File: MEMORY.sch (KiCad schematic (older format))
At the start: 2 parts

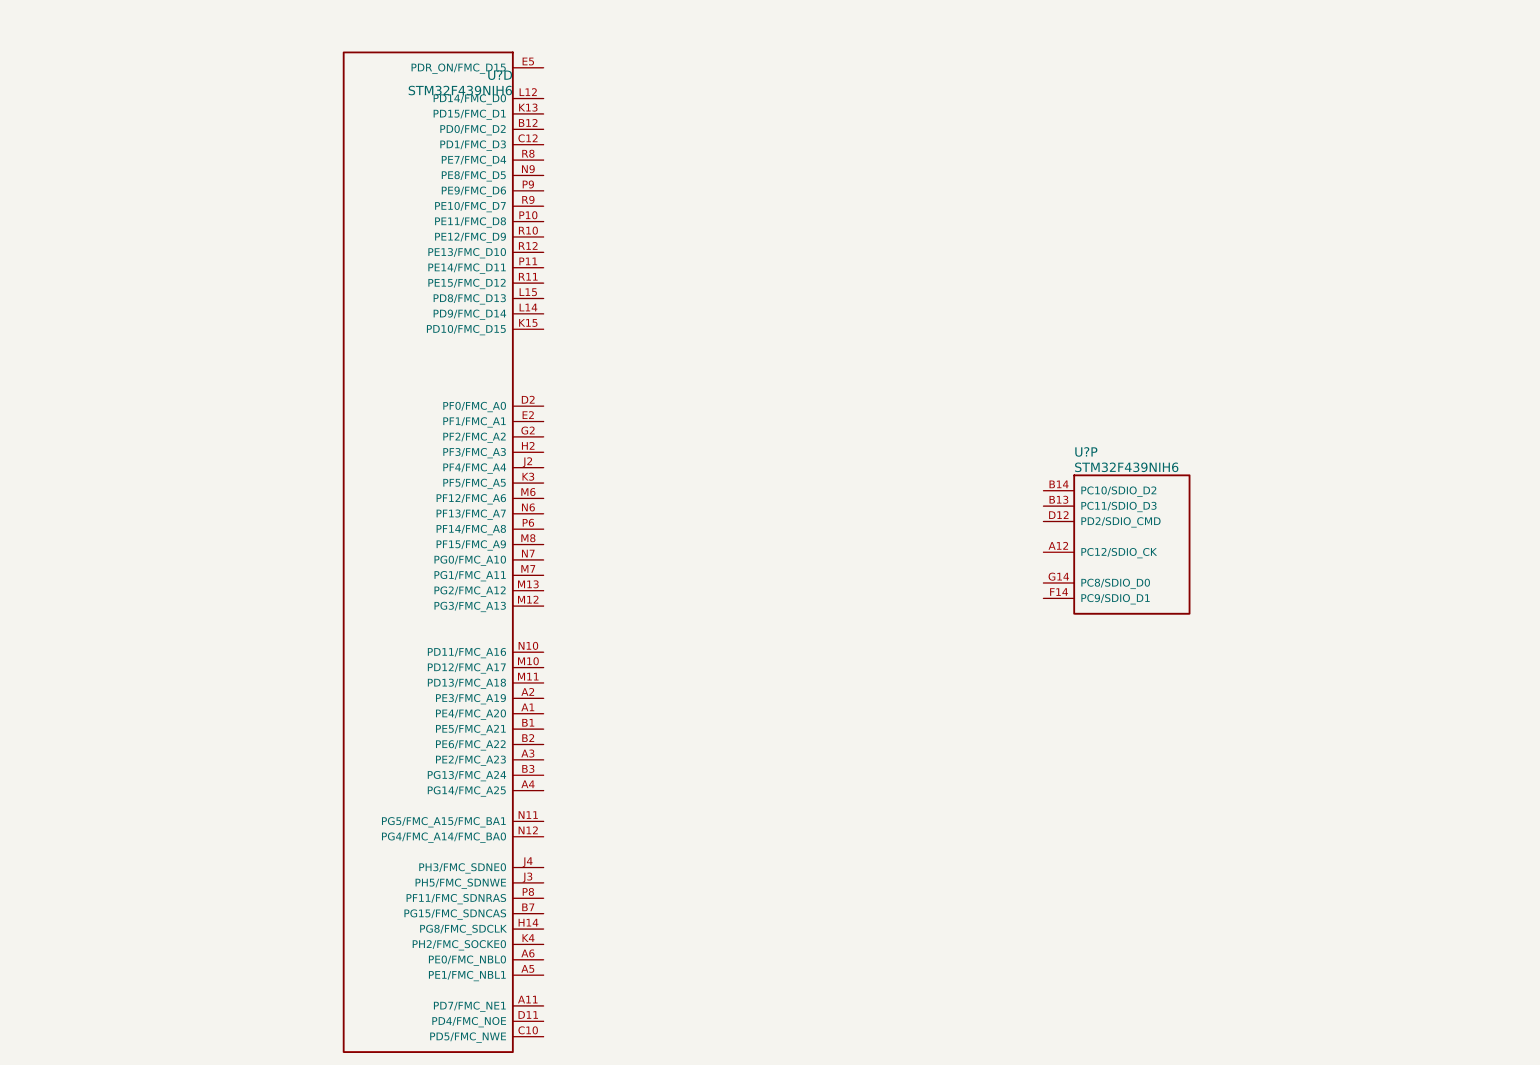
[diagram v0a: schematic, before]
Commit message: current version of the schematics. Audio circuits are still missing.
Audio curcuit topology
Audio from cellphone module is routed to STM
Audio from microphone is routed to STM
STM processes audio and routes microphone data to cellphone module
STM processes audio and routes cellphone audio to amplifier
analog multiplexer can switch route from mic directly to cellphone module and module to speaker
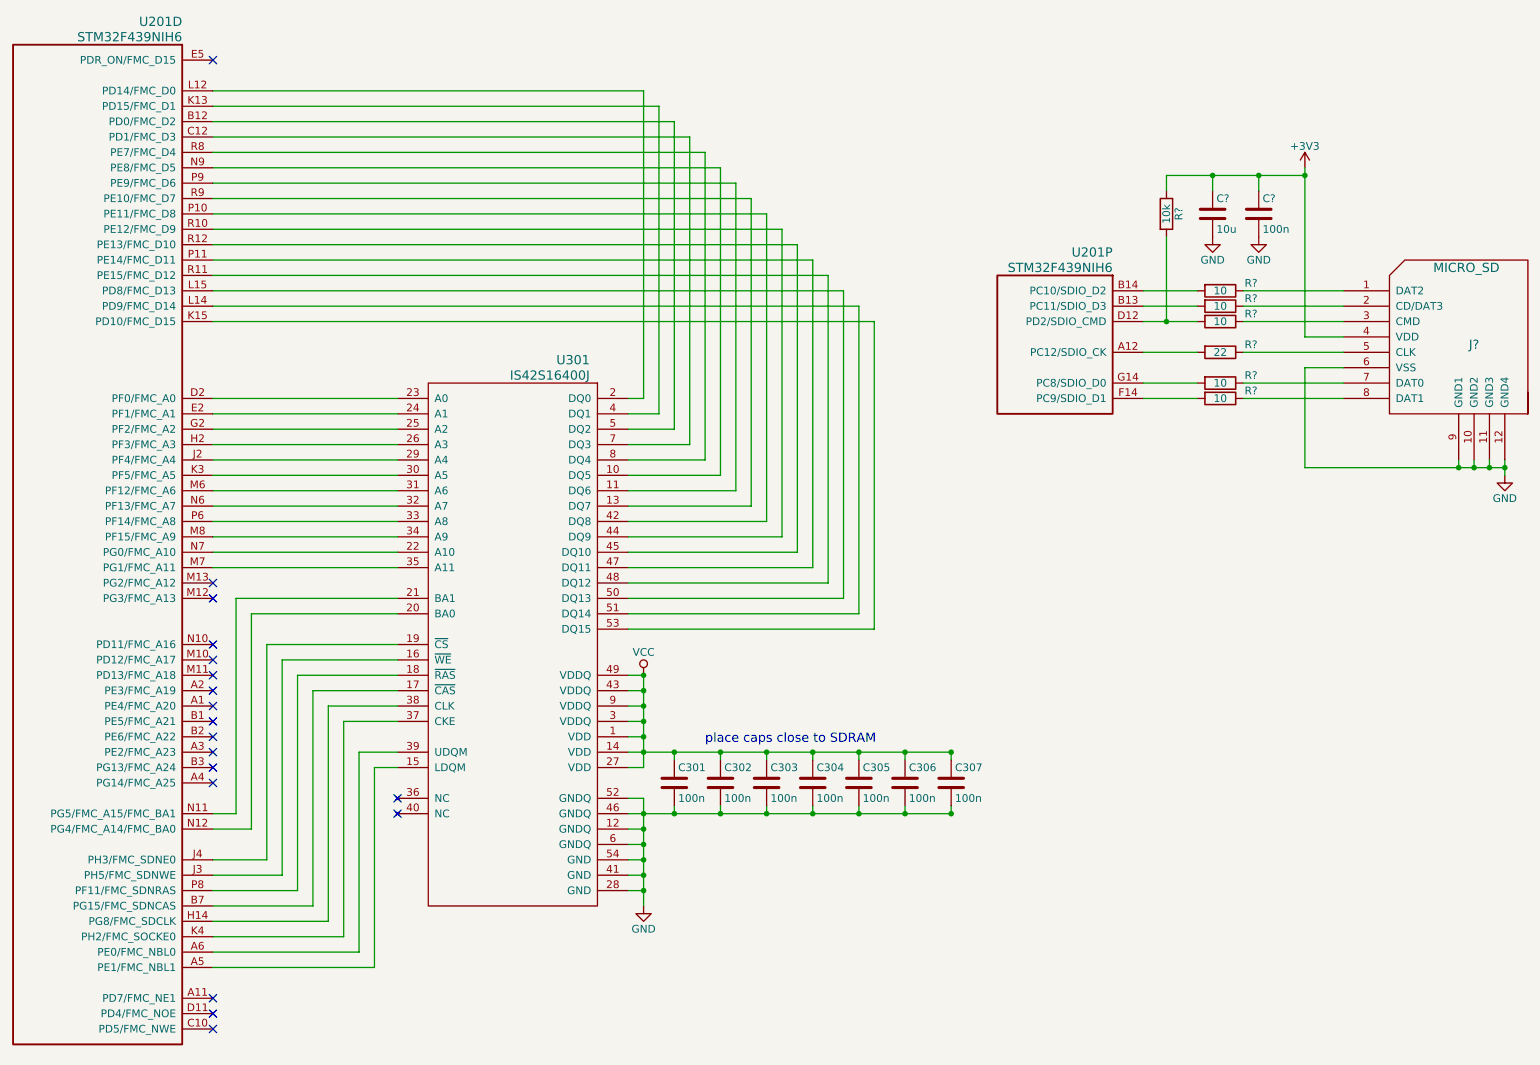
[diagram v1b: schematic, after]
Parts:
- added C301, C302, C303, C304, C305, C306, C307, C?: 100n, symbol C
- added C?: 10u, symbol C
- added J?: MICRO_SD, symbol MICRO_SD
- added R? (x5): 10, symbol R
- added R?: 22, symbol R
- added R?: 10k, symbol R
- added U301: IS42S16400J, symbol IS42S16400J
- gave numbers to parts that had none: 1
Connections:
- net at U201.A12 (PC12/SDIO_CK): now also R?.2
- net at U201.B13 (PC11/SDIO_D3): now also R?.2
- net at U201.B14 (PC10/SDIO_D2): now also R?.2
- net at U201.D12 (PD2/SDIO_CMD): now also R?.2, R?.2
- net at U201.F14 (PC9/SDIO_D1): now also R?.2
- net at U201.G14 (PC8/SDIO_D0): now also R?.2
- net at U201.A5 (PE1/FMC_NBL1): now also U301.15 (LDQM)
- net at U201.A6 (PE0/FMC_NBL0): now also U301.39 (UDQM)
- net at U201.B12 (PD0/FMC_D2): now also U301.5 (DQ2)
- net at U201.B7 (PG15/FMC_SDNCAS): now also U301.17 (~CAS)
- net at U201.C12 (PD1/FMC_D3): now also U301.7 (DQ3)
- net at U201.D2 (PF0/FMC_A0): now also U301.23 (A0)
- net at U201.E2 (PF1/FMC_A1): now also U301.24 (A1)
- net at U201.G2 (PF2/FMC_A2): now also U301.25 (A2)
- net at U201.H14 (PG8/FMC_SDCLK): now also U301.38 (CLK)
- net at U201.H2 (PF3/FMC_A3): now also U301.26 (A3)
- net at U201.J2 (PF4/FMC_A4): now also U301.29 (A4)
- net at U201.J3 (PH5/FMC_SDNWE): now also U301.16 (~WE)
- net at U201.J4 (PH3/FMC_SDNE0): now also U301.19 (~CS)
- net at U201.K13 (PD15/FMC_D1): now also U301.4 (DQ1)
- net at U201.K15 (PD10/FMC_D15): now also U301.53 (DQ15)
- net at U201.K3 (PF5/FMC_A5): now also U301.30 (A5)
- net at U201.K4 (PH2/FMC_SOCKE0): now also U301.37 (CKE)
- net at U201.L12 (PD14/FMC_D0): now also U301.2 (DQ0)
- net at U201.L14 (PD9/FMC_D14): now also U301.51 (DQ14)
- net at U201.L15 (PD8/FMC_D13): now also U301.50 (DQ13)
- net at U201.M6 (PF12/FMC_A6): now also U301.31 (A6)
- net at U201.M7 (PG1/FMC_A11): now also U301.35 (A11)
- net at U201.M8 (PF15/FMC_A9): now also U301.34 (A9)
- net at U201.N11 (PG5/FMC_A15/FMC_BA1): now also U301.21 (BA1)
- net at U201.N12 (PG4/FMC_A14/FMC_BA0): now also U301.20 (BA0)
- net at U201.N6 (PF13/FMC_A7): now also U301.32 (A7)
- net at U201.N7 (PG0/FMC_A10): now also U301.22 (A10)
- net at U201.N9 (PE8/FMC_D5): now also U301.10 (DQ5)
- net at U201.P10 (PE11/FMC_D8): now also U301.42 (DQ8)
- net at U201.P11 (PE14/FMC_D11): now also U301.47 (DQ11)
- net at U201.P6 (PF14/FMC_A8): now also U301.33 (A8)
- net at U201.P8 (PF11/FMC_SDNRAS): now also U301.18 (~RAS)
- net at U201.P9 (PE9/FMC_D6): now also U301.11 (DQ6)
- net at U201.R10 (PE12/FMC_D9): now also U301.44 (DQ9)
- net at U201.R11 (PE15/FMC_D12): now also U301.48 (DQ12)
- net at U201.R12 (PE13/FMC_D10): now also U301.45 (DQ10)
- net at U201.R8 (PE7/FMC_D4): now also U301.8 (DQ4)
- net at U201.R9 (PE10/FMC_D7): now also U301.13 (DQ7)
- new net: J?.1 (DAT2), R?.1
- new net: J?.2 (CD/DAT3), R?.1
- new net: J?.3 (CMD), R?.1
- new net: J?.5 (CLK), R?.1
- new net: J?.7 (DAT0), R?.1
- new net: J?.8 (DAT1), R?.1
- new net +3V3: C?.1, C?.1, J?.4 (VDD), R?.1
- new net GND: C301.2, C302.2, C303.2, C304.2, C305.2, C306.2, C307.2, C?.2, C?.2, J?.10 (GND2), J?.11 (GND3), J?.12 (GND4), J?.6 (VSS), J?.9 (GND1), U301.12 (GNDQ), U301.28 (GND), U301.41 (GND), U301.46 (GNDQ), U301.52 (GNDQ), U301.54 (GND), U301.6 (GNDQ)
- new net VCC: C301.1, C302.1, C303.1, C304.1, C305.1, C306.1, C307.1, U301.1 (VDD), U301.14 (VDD), U301.27 (VDD), U301.3 (VDDQ), U301.43 (VDDQ), U301.49 (VDDQ), U301.9 (VDDQ)
- no-connect marks 0 -> 18
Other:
- note added: "place caps close to SDRAM"
- moved on the sheet: U201D, U201P

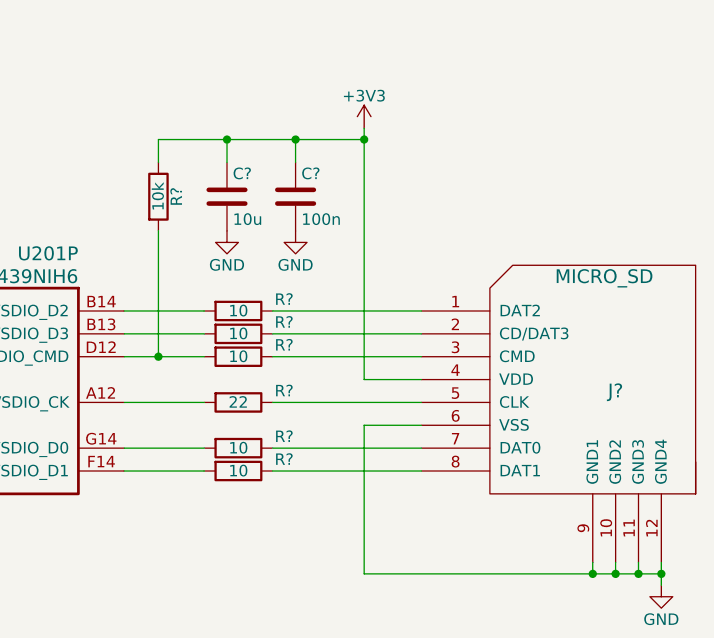
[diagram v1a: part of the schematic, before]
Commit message: added Ti WL1807/1837 Module for WLAN and Bluetooth. added Test Points
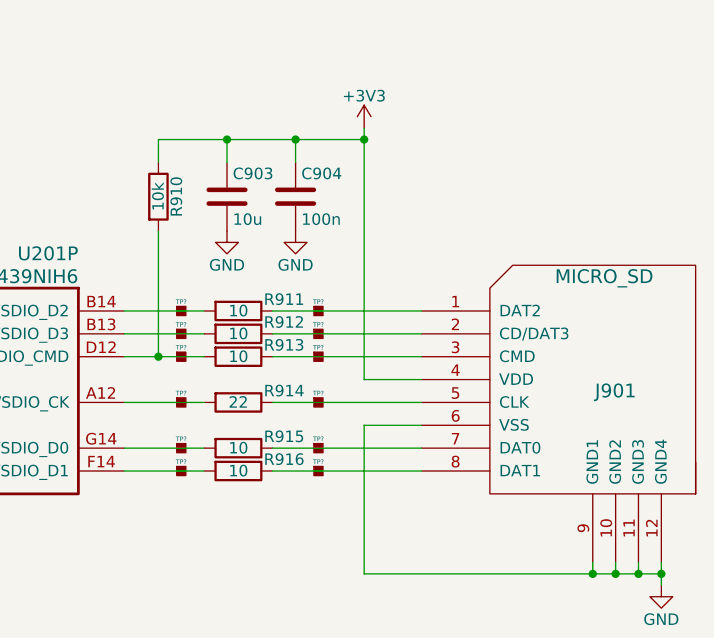
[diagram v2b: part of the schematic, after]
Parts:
- added TP? (x12): TP, symbol TP
- gave numbers to parts that had none: 10
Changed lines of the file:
@@
 LIBS:micro_sd
 LIBS:h144tc215a
-LIBS:3310retro-cache
+LIBS:WL1807MODGIMOCT
+LIBS:tp
+LIBS:w3006
+LIBS:3210retro-cache
 EELAYER 25 0
 EELAYER END
@@
 encoding utf-8
 Sheet 9 9
-Title "Nokia 3310 Retrofit"
-Date "2016-12-08"
+Title "Nokia 3210 Retrofit"
+Date "2016-12-20"
 Rev "1"
 Comp "www.kurzschluss-blog.de"
@@
 Connection ~ 4950 6000
 $Comp
-L GND #PWR302
+L GND #PWR902
 U 1 1 584DBACB
 P 4950 6600
-F 0 "#PWR302" H 4950 6350 50  0001 C CNN
+F 0 "#PWR902" H 4950 6350 50  0001 C CNN
 F 1 "GND" H 4950 6450 50  0000 C CNN
 F 2 "" H 4950 6600 50  0000 C CNN
@@
 Connection ~ 4950 6500
 $Comp
-L VCC #PWR301
+L VCC #PWR901
 U 1 1 584DBB5F
 P 4950 5100
-F 0 "#PWR301" H 4950 4950 50  0001 C CNN
+F 0 "#PWR901" H 4950 4950 50  0001 C CNN
 F 1 "VCC" H 4950 5250 50  0000 C CNN
 F 2 "" H 4950 5100 50  0000 C CNN
@@
 NoConn ~ 2150 7400
 $Comp
-L MICRO_SD J?
+L MICRO_SD J901
 U 1 1 584DD7A8
 P 10300 3000
-F 0 "J?" H 10350 3050 60  0000 C CNN
+F 0 "J901" H 10350 3050 60  0000 C CNN
 F 1 "MICRO_SD" H 10300 3550 60  0000 C CNN
 F 2 "" V 10410 2500 60  0000 C CNN
@@
 $EndComp
 $Comp
-L GND #PWR?
+L GND #PWR906
 U 1 1 584DD873
 P 10550 3800
-F 0 "#PWR?" H 10550 3550 50  0001 C CNN
+F 0 "#PWR906" H 10550 3550 50  0001 C CNN
 F 1 "GND" H 10550 3650 50  0000 C CNN
 F 2 "" H 10550 3800 50  0000 C CNN
@@
 	9500 2600 8850 2600
 $Comp
-L R R?
+L R R911
 U 1 1 584DE0FD
 P 8700 2600
-F 0 "R?" V 8650 2800 50  0000 C CNN
+F 0 "R911" V 8650 2800 50  0000 C CNN
 F 1 "10" V 8700 2600 50  0000 C CNN
 F 2 "" V 8630 2600 50  0000 C CNN
@@
 $EndComp
 $Comp
-L R R?
+L R R912
 U 1 1 584DE1D3
 P 8700 2700
-F 0 "R?" V 8650 2900 50  0000 C CNN
+F 0 "R912" V 8650 2900 50  0000 C CNN
 F 1 "10" V 8700 2700 50  0000 C CNN
 F 2 "" V 8630 2700 50  0000 C CNN
@@
 $EndComp
 $Comp
-L R R?
+L R R913
 U 1 1 584DE20A
 P 8700 2800
-F 0 "R?" V 8650 3000 50  0000 C CNN
+F 0 "R913" V 8650 3000 50  0000 C CNN
 F 1 "10" V 8700 2800 50  0000 C CNN
 F 2 "" V 8630 2800 50  0000 C CNN
@@
 $EndComp
 $Comp
-L R R?
+L R R914
 U 1 1 584DE252
 P 8700 3000
-F 0 "R?" V 8650 3200 50  0000 C CNN
+F 0 "R914" V 8650 3200 50  0000 C CNN
 F 1 "22" V 8700 3000 50  0000 C CNN
 F 2 "" V 8630 3000 50  0000 C CNN
@@
 $EndComp
 $Comp
-L R R?
+L R R915
 U 1 1 584DE2C4
 P 8700 3200
-F 0 "R?" V 8650 3400 50  0000 C CNN
+F 0 "R915" V 8650 3400 50  0000 C CNN
 F 1 "10" V 8700 3200 50  0000 C CNN
 F 2 "" V 8630 3200 50  0000 C CNN
@@
 $EndComp
 $Comp
-L R R?
+L R R916
 U 1 1 584DE318
 P 8700 3300
-F 0 "R?" V 8650 3500 50  0000 C CNN
+F 0 "R916" V 8650 3500 50  0000 C CNN
 F 1 "10" V 8700 3300 50  0000 C CNN
 F 2 "" V 8630 3300 50  0000 C CNN
@@
 	8550 2600 8200 2600
 $Comp
-L +3V3 #PWR?
+L +3V3 #PWR905
 U 1 1 584E0DE7
 P 9250 1800
-F 0 "#PWR?" H 9250 1650 50  0001 C CNN
+F 0 "#PWR905" H 9250 1650 50  0001 C CNN
 F 1 "+3V3" H 9250 1940 50  0000 C CNN
 F 2 "" H 9250 1800 50  0000 C CNN
@@
 $EndComp
 $Comp
-L C C?
+L C C904
 U 1 1 584E0F4B
 P 8950 2100
-F 0 "C?" H 8975 2200 50  0000 L CNN
+F 0 "C904" H 8975 2200 50  0000 L CNN
 F 1 "100n" H 8975 2000 50  0000 L CNN
 F 2 "" H 8988 1950 50  0000 C CNN
@@
 $EndComp
 $Comp
-L C C?
+L C C903
 U 1 1 584E0FEB
 P 8650 2100
-F 0 "C?" H 8675 2200 50  0000 L CNN
+F 0 "C903" H 8675 2200 50  0000 L CNN
 F 1 "10u" H 8675 2000 50  0000 L CNN
 F 2 "" H 8688 1950 50  0000 C CNN
@@
 Connection ~ 8650 1850
 $Comp
-L R R?
+L R R910
 U 1 1 584E1303
 P 8350 2100
-F 0 "R?" V 8430 2100 50  0000 C CNN
+F 0 "R910" V 8430 2100 50  0000 C CNN
 F 1 "10k" V 8350 2100 50  0000 C CNN
 F 2 "" V 8280 2100 50  0000 C CNN
@@
 Connection ~ 8350 2800
 $Comp
-L GND #PWR?
+L GND #PWR904
 U 1 1 584E1578
 P 8950 2250
-F 0 "#PWR?" H 8950 2000 50  0001 C CNN
+F 0 "#PWR904" H 8950 2000 50  0001 C CNN
 F 1 "GND" H 8950 2100 50  0000 C CNN
 F 2 "" H 8950 2250 50  0000 C CNN
@@
 $EndComp
 $Comp
-L GND #PWR?
+L GND #PWR903
 U 1 1 584E15BF
 P 8650 2250
-F 0 "#PWR?" H 8650 2000 50  0001 C CNN
+F 0 "#PWR903" H 8650 2000 50  0001 C CNN
 F 1 "GND" H 8650 2100 50  0000 C CNN
 F 2 "" H 8650 2250 50  0000 C CNN
@@
 NoConn ~ 2150 5800
 NoConn ~ 2150 1100
+$Comp
+L TP TP?
+U 1 1 585C79CD
+P 8450 2600
+F 0 "TP?" H 8450 2640 20  0000 C CNN
+F 1 "TP" H 8450 2550 60  0001 C CNN
+F 2 "" H 8450 2600 60  0000 C CNN
+F 3 "" H 8450 2600 60  0000 C CNN
+	1    8450 2600
+	1    0    0    -1
+$EndComp
+$Comp
+L TP TP?
+U 1 1 585C7A1F
+P 8450 2700
+F 0 "TP?" H 8450 2740 20  0000 C CNN
+F 1 "TP" H 8450 2650 60  0001 C CNN
+F 2 "" H 8450 2700 60  0000 C CNN
+F 3 "" H 8450 2700 60  0000 C CNN
+	1    8450 2700
+	1    0    0    -1
+$EndComp
+$Comp
+L TP TP?
+U 1 1 585C7A75
+P 8450 2800
+F 0 "TP?" H 8450 2840 20  0000 C CNN
+F 1 "TP" H 8450 2750 60  0001 C CNN
+F 2 "" H 8450 2800 60  0000 C CNN
+F 3 "" H 8450 2800 60  0000 C CNN
+	1    8450 2800
+	1    0    0    -1
+$EndComp
+$Comp
+L TP TP?
+U 1 1 585C7ACE
+P 8450 3000
+F 0 "TP?" H 8450 3040 20  0000 C CNN
+F 1 "TP" H 8450 2950 60  0001 C CNN
+F 2 "" H 8450 3000 60  0000 C CNN
+F 3 "" H 8450 3000 60  0000 C CNN
+	1    8450 3000
+	1    0    0    -1
+$EndComp
+$Comp
+L TP TP?
+U 1 1 585C7B32
+P 8450 3200
+F 0 "TP?" H 8450 3240 20  0000 C CNN
+F 1 "TP" H 8450 3150 60  0001 C CNN
+F 2 "" H 8450 3200 60  0000 C CNN
+F 3 "" H 8450 3200 60  0000 C CNN
+	1    8450 3200
+	1    0    0    -1
+$EndComp
+$Comp
+L TP TP?
+U 1 1 585C7B9D
+P 8450 3300
+F 0 "TP?" H 8450 3340 20  0000 C CNN
+F 1 "TP" H 8450 3250 60  0001 C CNN
+F 2 "" H 8450 3300 60  0000 C CNN
+F 3 "" H 8450 3300 60  0000 C CNN
+	1    8450 3300
+	1    0    0    -1
+$EndComp
+$Comp
+L TP TP?
+U 1 1 585C7BFF
+P 9050 3300
+F 0 "TP?" H 9050 3340 20  0000 C CNN
+F 1 "TP" H 9050 3250 60  0001 C CNN
+F 2 "" H 9050 3300 60  0000 C CNN
+F 3 "" H 9050 3300 60  0000 C CNN
+	1    9050 3300
+	1    0    0    -1
+$EndComp
+$Comp
+L TP TP?
+U 1 1 585C7C8C
+P 9050 3200
+F 0 "TP?" H 9050 3240 20  0000 C CNN
+F 1 "TP" H 9050 3150 60  0001 C CNN
+F 2 "" H 9050 3200 60  0000 C CNN
+F 3 "" H 9050 3200 60  0000 C CNN
+	1    9050 3200
+	1    0    0    -1
+$EndComp
+$Comp
+L TP TP?
+U 1 1 585C7D52
+P 9050 3000
+F 0 "TP?" H 9050 3040 20  0000 C CNN
+F 1 "TP" H 9050 2950 60  0001 C CNN
+F 2 "" H 9050 3000 60  0000 C CNN
+F 3 "" H 9050 3000 60  0000 C CNN
+	1    9050 3000
+	1    0    0    -1
+$EndComp
+$Comp
+L TP TP?
+U 1 1 585C7DC5
+P 9050 2800
+F 0 "TP?" H 9050 2840 20  0000 C CNN
+F 1 "TP" H 9050 2750 60  0001 C CNN
+F 2 "" H 9050 2800 60  0000 C CNN
+F 3 "" H 9050 2800 60  0000 C CNN
+	1    9050 2800
+	1    0    0    -1
+$EndComp
+$Comp
+L TP TP?
+U 1 1 585C7EC1
+P 9050 2700
+F 0 "TP?" H 9050 2740 20  0000 C CNN
+F 1 "TP" H 9050 2650 60  0001 C CNN
+F 2 "" H 9050 2700 60  0000 C CNN
+F 3 "" H 9050 2700 60  0000 C CNN
+	1    9050 2700
+	1    0    0    -1
+$EndComp
+$Comp
+L TP TP?
+U 1 1 585C7F32
+P 9050 2600
+F 0 "TP?" H 9050 2640 20  0000 C CNN
+F 1 "TP" H 9050 2550 60  0001 C CNN
+F 2 "" H 9050 2600 60  0000 C CNN
+F 3 "" H 9050 2600 60  0000 C CNN
+	1    9050 2600
+	1    0    0    -1
+$EndComp
 $EndSCHEMATC
